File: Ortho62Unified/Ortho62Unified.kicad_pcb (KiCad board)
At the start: 2 copper layers, 300 x 140 mm, 185 parts, among them J1 AVR-PDI-6, J2 Conn_01x06_Socket, J3 USB_C_Receptacle_USB2.0, J4 Conn_01x08_Socket, J5 Conn_01x06_Socket, SW1 SW_Push, SW10 SW_Push, SW11 SW_Push, SW12 SW_Push, SW13 SW_Push, SW14 SW_Push, SW15 SW_Push, SW16 SW_Push, SW17 SW_Push, SW18 SW_Push, SW19 SW_Push, SW2 SW_Push, SW20 SW_Push, SW21 SW_Push, SW22 SW_Push, SW23 SW_Push, SW24 SW_Push, SW25 SW_Push, SW26 SW_Push, SW27 SW_Push, SW28 SW_Push, SW29 SW_Push, SW3 SW_Push, SW30 SW_Push, SW31 SW_Push, SW32 SW_Push, SW33 SW_Push, SW34 SW_Push, SW35 SW_Push, SW36 SW_Push, SW37 SW_Push, SW38 SW_Push, SW39 SW_Push, SW4 SW_Push, SW40 SW_Push, SW41 SW_Push, SW42 SW_Push, SW43 SW_Push, SW44 SW_Push, SW45 SW_Push, SW46 SW_Push, SW47 SW_Push, SW48 SW_Push, SW49 SW_Push, SW5 SW_Push, SW50 SW_Push, SW51 SW_Push, SW52 SW_Push, SW53 SW_Push, SW54 SW_Push, SW55 SW_Push, SW56 SW_Push, SW57 SW_Push, SW58 SW_Push, SW59 SW_Push, SW6 SW_Push, SW60 SW_Push, SW61 SW_Push, SW62 SW_Push, SW63 SW_Push, SW64 SW_Push, SW65 SW_Push, SW66 SW_Push, SW67 SW_Push, SW68 SW_Push, SW69 SW_Push, SW7 SW_Push, SW70 SW_Push, SW71 SW_Push, SW72 SW_Push, SW73 SW_Push, SW74 SW_Push, SW75 SW_Push, SW76 SW_Push, SW77 SW_Push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

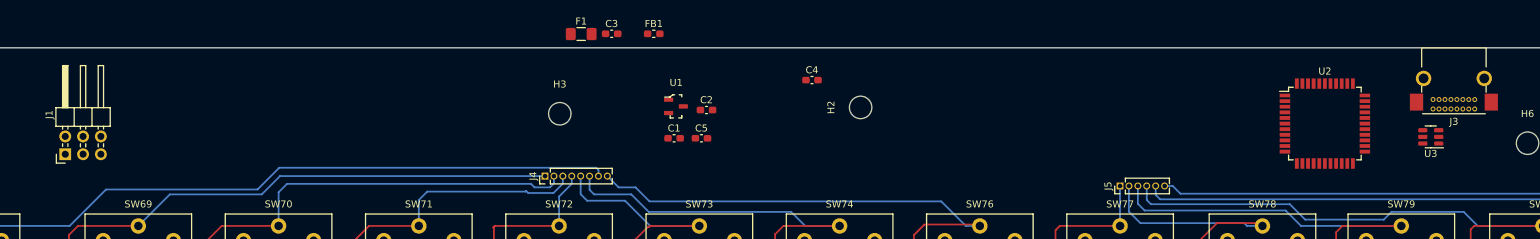
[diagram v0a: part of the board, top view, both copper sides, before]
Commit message: Consolitate and place Xmega and USB components.
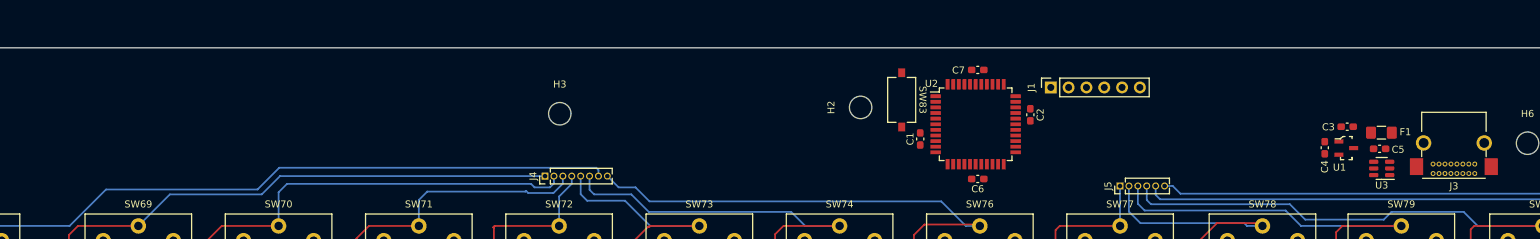
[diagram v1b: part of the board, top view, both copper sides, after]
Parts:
- removed FB1: FerriteBead, Inductor_SMD:L_0603_1608Metric_Pad1.05x0.95mm_HandSolder
- added C6: C, Capacitor_SMD:C_0603_1608Metric_Pad1.08x0.95mm_HandSolder, F.Cu at (199.6, 52.4)
- added C7: C, Capacitor_SMD:C_0603_1608Metric_Pad1.08x0.95mm_HandSolder, F.Cu at (199.6, 36.9)
- added SW83: SW_Push, Button_Switch_SMD:SW_Tactile_SPST_NO_Straight_CK_PTS636Sx25SMTRLFS, F.Cu at (188.8, 41.1)
- J1: footprint Connector_PinHeader_2.54mm:PinHeader_2x03_P2.54mm_Horizontal -> Connector_PinSocket_2.54mm:PinSocket_1x06_P2.54mm_Vertical
- moved J1 140.9 mm to (210.0, 39.4)
- moved F1 115.0 mm to (257.2, 45.8), turned to 180 degrees
- moved C3 105.7 mm to (252.3, 45.0), turned to 180 degrees
- moved C5 96.7 mm to (256.9, 48.1), turned to 180 degrees
- moved U1 95.8 mm to (252.2, 48.0)
- moved C4 73.8 mm to (249.1, 48.0), turned to 90 degrees
- moved U2 49.8 mm to (199.3, 44.6)
- moved C2 46.2 mm to (207.1, 43.2), turned to -90 degrees
- moved C1 35.1 mm to (191.4, 46.7), turned to 90 degrees
- moved J3 9.20 mm to (270.5, 51.6)
- moved U3 8.32 mm to (257.2, 50.9)
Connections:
- C2 pad 1: Net-(U2-AVCC) -> +3V3
- U2 pad 39: Net-(U2-AVCC) -> +3V3

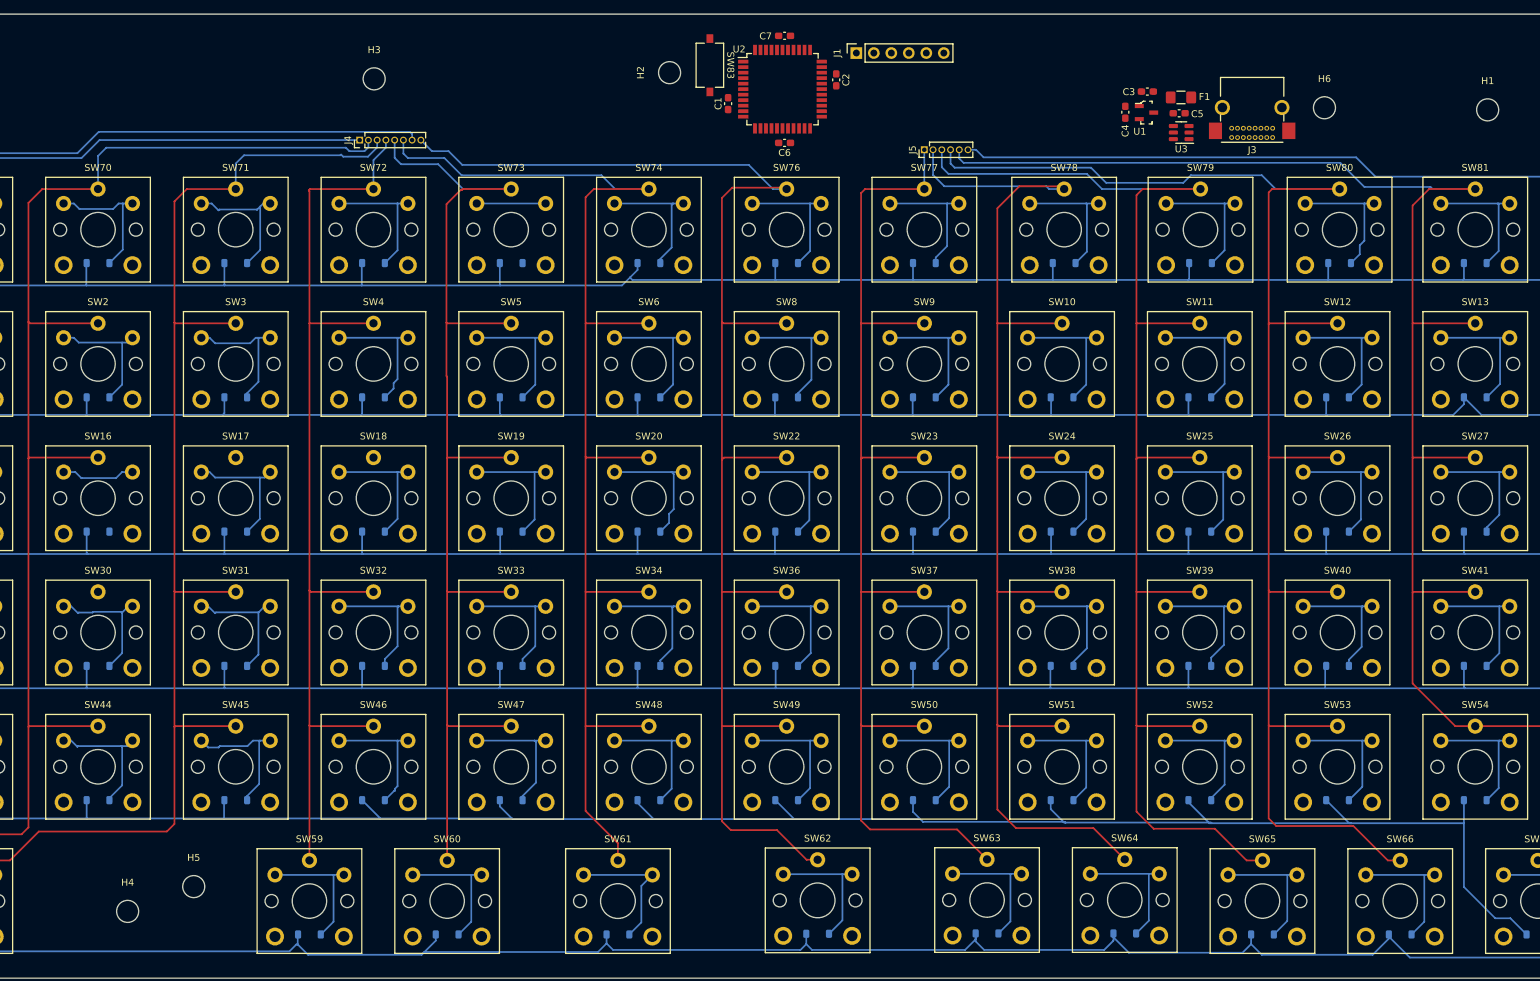
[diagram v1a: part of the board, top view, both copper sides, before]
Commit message: Remove F6,F7,F8 keys to create space for controller.
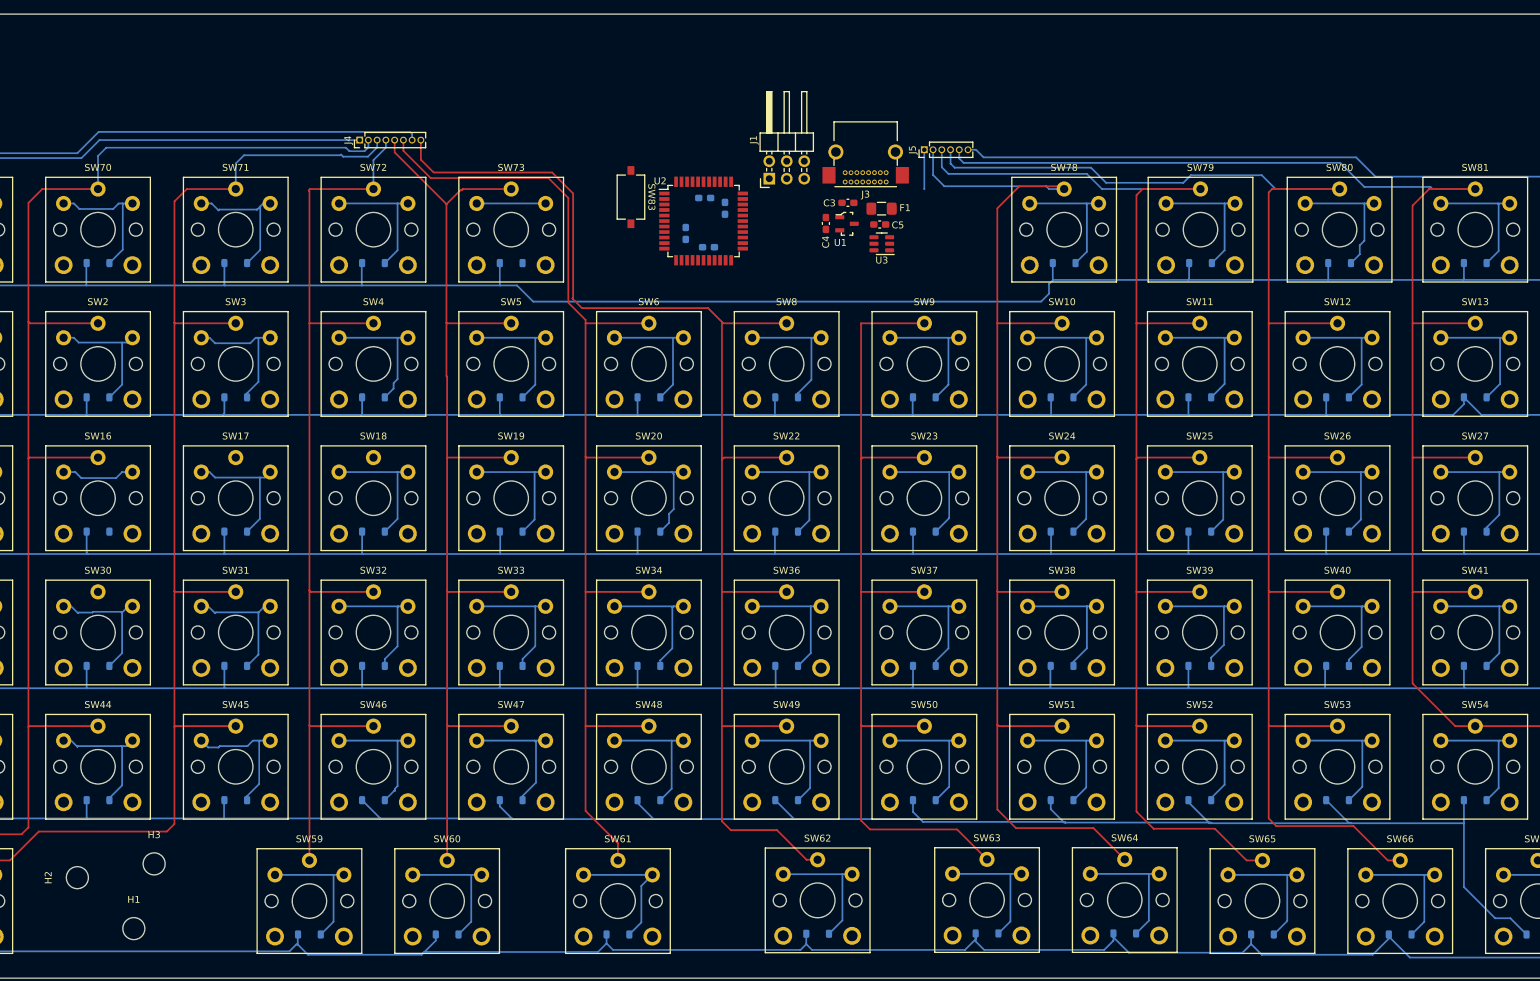
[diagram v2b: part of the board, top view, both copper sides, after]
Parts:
- removed D74, D76, D77: 1N4148W, Diode_SMD:D_SOD-123
- removed H4, H5, H6: MountingHole, MountingHole:MountingHole_3.2mm_M3
- removed SW74, SW76, SW77: SW_Push, Switch_Keyboard_Kailh:SW_Kailh_Choc_V1V2_1.00u
- C1, C2, C6, C7: moved to B.Cu
- J1: footprint Connector_PinSocket_2.54mm:PinSocket_1x06_P2.54mm_Vertical -> Connector_PinHeader_2.54mm:PinHeader_2x03_P2.54mm_Horizontal
- moved H1 229.8 mm to (105.1, 166.5)
- moved H2 145.1 mm to (96.9, 159.1)
- moved H3 118.4 mm to (108.0, 157.1)
- moved J3 56.5 mm to (214.3, 58.1)
- moved F1 46.4 mm to (213.7, 62.0)
- moved U1 46.4 mm to (208.7, 64.2)
- moved C4 46.4 mm to (205.6, 64.1)
- moved C3 46.4 mm to (208.8, 61.1)
- moved C5 46.4 mm to (213.4, 64.2)
- moved U3 46.4 mm to (213.7, 67.0)
- moved C7 26.3 mm to (188.0, 60.4)
- moved C2 24.7 mm to (190.9, 61.9)
- moved SW83 22.3 mm to (177.3, 60.3)
- moved U2 22.3 mm to (187.8, 63.8)
- moved J1 22.2 mm to (197.4, 57.6)
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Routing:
- net /COL_8: track 163.9 -> 135.5 mm
- net /COL_5: track 184.5 -> 164.4 mm
- net Net-(D74-A): track 19.4 -> 0.00 mm
- net Net-(D76-A): track 19.4 -> 0.00 mm
- net Net-(D77-A): track 19.3 -> 0.00 mm
- net /COL_7: track 210.7 -> 191.9 mm
- net /COL_4: track 164.5 -> 155.5 mm
- net /ROW_F: track 326.1 -> 321.1 mm

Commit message: Progress routing rows and columns.
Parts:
- removed J1: AVR-PDI-6, Connector_PinHeader_2.54mm:PinHeader_2x03_P2.54mm_Horizontal
- removed J4: Conn_01x08_Socket, Connector_PinHeader_1.27mm:PinHeader_1x08_P1.27mm_Vertical
- added D74: Green, LED_SMD:LED_0805_2012Metric_Pad1.15x1.40mm_HandSolder, F.Cu at (199.7, 63.7)
- added D76: Red, LED_SMD:LED_0805_2012Metric_Pad1.15x1.40mm_HandSolder, F.Cu at (179.6, 64.5)
- added J6: Conn_01x06_Socket, Connector_PinHeader_1.27mm:PinHeader_1x06_P1.27mm_Vertical, F.Cu at (186.9, 73.5)
- added J7: Conn_01x08_Socket, Connector_PinHeader_1.27mm:PinHeader_1x08_P1.27mm_Vertical, F.Cu at (172.8, 57.7)
- added J8: Conn_01x06_Socket, Connector_PinHeader_1.27mm:PinHeader_1x06_P1.27mm_Vertical, F.Cu at (196.8, 73.8)
- added J9: TC2030-IDC-NL, Tag_Connect:TC2030-IDC-NL, F.Cu at (198.3, 58.3)
- added R1: 499, Resistor_SMD:R_0805_2012Metric_Pad1.20x1.40mm_HandSolder, F.Cu at (202.2, 63.7)
- added R2: 499, LED_SMD:LED_0805_2012Metric_Pad1.15x1.40mm_HandSolder, F.Cu at (177.2, 64.4)
- moved SW83 29.5 mm to (206.8, 59.0), turned to 0 degrees
- moved J5 17.5 mm to (226.2, 69.8), turned to -90 degrees
- moved J3 8.67 mm to (222.5, 61.0)
- moved C4 1.85 mm to (205.6, 66.0)
- moved U3 1.85 mm to (213.7, 68.9)
- moved C3 1.85 mm to (208.8, 63.0)
- moved C5 1.85 mm to (213.4, 66.1)
- moved F1 1.85 mm to (213.7, 63.8)
- moved U1 1.85 mm to (208.7, 66.0)
- moved C6 1.15 mm to (188.4, 66.4)
- moved C7 0.35 mm to (188.0, 60.8)
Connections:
- J3 pad S1: unconnected-(J3-SHIELD-PadS1) -> GND
- U2 pad 1: unconnected-(U2-PA5-Pad1) -> /COL_5
- U2 pad 10: unconnected-(U2-PC0-Pad10) -> /ROW_4
- U2 pad 11: unconnected-(U2-PC1-Pad11) -> /ROW_3
- U2 pad 12: unconnected-(U2-PC2-Pad12) -> /ROW_2
- U2 pad 13: unconnected-(U2-PC3-Pad13) -> /ROW_1
- U2 pad 14: unconnected-(U2-PC4-Pad14) -> /ROW_0
- U2 pad 15: unconnected-(U2-PC5-Pad15) -> /ROW_F
- U2 pad 2: unconnected-(U2-PA6-Pad2) -> /COL_6
- U2 pad 20: unconnected-(U2-PD0-Pad20) -> /COL_8
- U2 pad 21: unconnected-(U2-PD1-Pad21) -> /COL_9
- U2 pad 22: unconnected-(U2-PD2-Pad22) -> /COL_10
- U2 pad 23: unconnected-(U2-PD3-Pad23) -> /COL_11
- U2 pad 24: unconnected-(U2-PD4-Pad24) -> /COL_12
- U2 pad 25: unconnected-(U2-PD5-Pad25) -> /COL_13
- U2 pad 3: unconnected-(U2-PA7-Pad3) -> /COL_7
- U2 pad 40: unconnected-(U2-AREFA/PA0-Pad40) -> /COL_0
- U2 pad 41: unconnected-(U2-PA1-Pad41) -> /COL_1
- U2 pad 42: unconnected-(U2-PA2-Pad42) -> /COL_2
- U2 pad 43: unconnected-(U2-PA3-Pad43) -> /COL_3
- U2 pad 44: unconnected-(U2-PA4-Pad44) -> /COL_4
- U2 pad 7: unconnected-(U2-PB3-Pad7) -> Net-(U2-PB3)
- U3 pad 1: /USB_D- -> /USB_D+
- U3 pad 3: /USB_D+ -> /USB_D-
- U3 pad 4: /USBM+ -> /USBM-
- U3 pad 6: /USBM- -> /USBM+
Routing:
- net /COL_6: track 181.7 -> 237.4 mm, vias 0 -> 2
- net /COL_0: track 202.8 -> 256.1 mm
- net +3V3: track 0.00 -> 49.8 mm, vias 0 -> 4
- net /COL_13: track 250.2 -> 294.1 mm
- net /COL_12: track 221.0 -> 262.5 mm
- net /COL_11: track 224.2 -> 264.4 mm
- net /COL_10: track 198.8 -> 238.3 mm
- net /COL_9: track 181.3 -> 219.5 mm
- net /COL_8: track 135.5 -> 168.3 mm
- net /COL_1: track 210.0 -> 180.5 mm
- net /USBM+: track 0.00 -> 21.5 mm, vias 0 -> 2
- net /USBM-: track 0.00 -> 20.7 mm
- net /COL_7: track 191.9 -> 174.5 mm
- net /COL_5: track 164.4 -> 148.2 mm
- net /COL_4: track 155.5 -> 171.4 mm, vias 0 -> 1
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- added copper zone on B.Cu, net GND
- added copper zone on F.Cu, net GND

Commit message: Routing complete for Xmega based design.
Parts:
- U1: footprint digikey-footprints:SOT-23-3 -> Package_TO_SOT_SMD:SOT-23-3
- moved SW68 0.10 mm to (329.0, 162.5)
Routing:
- net /ROW_4: track 455.2 -> 583.0 mm, vias 0 -> 2
- net /ROW_3: track 410.1 -> 514.7 mm, vias 0 -> 2
- net /COL_1: track 180.5 -> 266.6 mm
- net /ROW_2: track 398.5 -> 468.9 mm, vias 0 -> 3
- net /COL_2: track 175.9 -> 241.1 mm
- net /ROW_1: track 376.1 -> 437.3 mm, vias 0 -> 1
- net /COL_3: track 149.3 -> 195.7 mm
- net /ROW_0: track 346.8 -> 387.3 mm, vias 0 -> 1
- net Net-(D73-A): track 10.0 -> 19.4 mm
- net Net-(D16-A): track 10.8 -> 19.9 mm
- net Net-(J9-Pin_5): track 7.94 -> 17.0 mm
- net /VBUS: track 13.7 -> 19.5 mm
- net /ROW_F: track 325.3 -> 327.4 mm
- net GND: vias 11 -> 12
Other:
- board text removed: "LEFT"
- board text removed: "RIGHT"

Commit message: Add fiducials on PCB.
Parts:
- added FIDU: Fiducial_0.5mm_Mask1mm, Fiducial:Fiducial_0.5mm_Mask1mm, F.Cu at (195.0, 53.5)
- added FIDU: Fiducial_0.5mm_Mask1mm, Fiducial:Fiducial_0.5mm_Mask1mm, F.Cu at (337.5, 172.0)
- added FIDU: Fiducial_0.5mm_Mask1mm, Fiducial:Fiducial_0.5mm_Mask1mm, F.Cu at (40.5, 171.5)
- added FIDU: Fiducial_0.5mm_Mask1mm, Fiducial:Fiducial_0.5mm_Mask1mm, F.Cu at (195.0, 172.0)
- added FIDU: Fiducial_0.5mm_Mask1mm, Fiducial:Fiducial_0.5mm_Mask1mm, F.Cu at (337.5, 53.5)
- added FIDU: Fiducial_0.5mm_Mask1mm, Fiducial:Fiducial_0.5mm_Mask1mm, F.Cu at (40.5, 53.0)
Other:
- board size 300 x 140 mm -> 300 x 121.8 mm
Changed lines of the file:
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@@
     )
     (pad_to_mask_clearance 0)
-    (aux_axis_origin 97.8 39.3)
+    (aux_axis_origin 55.4 65)
+    (grid_origin 41 0)
     (pcbplotparams
       (layerselection 0x00010fc_ffffffff)
@@
     )
   )
+  (footprint "Fiducial:Fiducial_0.5mm_Mask1mm" (layer "F.Cu")
+    (at 195 53.5)
+    (descr "Circular Fiducial, 0.5mm bare copper, 1mm soldermask opening (Level C)")
+    (tags "fiducial")
+    (attr smd)
+    (fp_text reference "FIDU" (at 3 0) (layer "F.SilkS")
+        (effects (font (size 1 1) (thickness 0.15)))
+    )
+    (fp_text value "Fiducial_0.5mm_Mask1mm" (at 0 1.5) (layer "F.Fab")
+        (effects (font (size 1 1) (thickness 0.15)))
+    )
+    (fp_text user "${REFERENCE}" (at 0 0) (layer "F.Fab")
+        (effects (font (size 0.2 0.2) (thickness 0.04)))
+    )
+    (fp_circle (center 0 0) (end 0.75 0)
+      (stroke (width 0.05) (type solid)) (fill none) (layer "F.CrtYd"))
+    (fp_circle (center 0 0) (end 0.5 0)
+      (stroke (width 0.1) (type solid)) (fill none) (layer "F.Fab"))
+    (pad "" smd circle (at 0 0) (size 0.5 0.5) (layers "F.Cu" "F.Mask")
+      (solder_mask_margin 0.25) (clearance 0.25))
+  )
   (footprint "Switch_Keyboard_Kailh:SW_Kailh_Choc_V1V2_1.00u" (layer "F.Cu")
     (at 99.9 65)
@@
     )
   )
+  (footprint "Fiducial:Fiducial_0.5mm_Mask1mm" (layer "F.Cu")
+    (at 337.5 172)
+    (descr "Circular Fiducial, 0.5mm bare copper, 1mm soldermask opening (Level C)")
+    (tags "fiducial")
+    (attr smd)
+    (fp_text reference "FIDU" (at -2.5 0) (layer "F.SilkS")
+        (effects (font (size 1 1) (thickness 0.15)))
+    )
+    (fp_text value "Fiducial_0.5mm_Mask1mm" (at 0 1.5) (layer "F.Fab")
+        (effects (font (size 1 1) (thickness 0.15)))
+    )
+    (fp_text user "${REFERENCE}" (at 0 0) (layer "F.Fab")
+        (effects (font (size 0.2 0.2) (thickness 0.04)))
+    )
+    (fp_circle (center 0 0) (end 0.75 0)
+      (stroke (width 0.05) (type solid)) (fill none) (layer "F.CrtYd"))
+    (fp_circle (center 0 0) (end 0.5 0)
+      (stroke (width 0.1) (type solid)) (fill none) (layer "F.Fab"))
+    (pad "" smd circle (at 0 0) (size 0.5 0.5) (layers "F.Cu" "F.Mask")
+      (solder_mask_margin 0.25) (clearance 0.25))
+  )
   (footprint "Switch_Keyboard_Kailh:SW_Kailh_Choc_V1V2_1.00u" (layer "F.Cu")
     (at 329 162.5)
@@
     )
   )
+  (footprint "Fiducial:Fiducial_0.5mm_Mask1mm" (layer "F.Cu")
+    (at 40.5 171.5)
+    (descr "Circular Fiducial, 0.5mm bare copper, 1mm soldermask opening (Level C)")
+    (tags "fiducial")
+    (attr smd)
+    (fp_text reference "FIDU" (at 3 0) (layer "F.SilkS")
+        (effects (font (size 1 1) (thickness 0.15)))
+    )
+    (fp_text value "Fiducial_0.5mm_Mask1mm" (at 0 1.5) (layer "F.Fab")
+        (effects (font (size 1 1) (thickness 0.15)))
+    )
+    (fp_text user "${REFERENCE}" (at 0 0) (layer "F.Fab")
+        (effects (font (size 0.2 0.2) (thickness 0.04)))
+    )
+    (fp_circle (center 0 0) (end 0.75 0)
+      (stroke (width 0.05) (type solid)) (fill none) (layer "F.CrtYd"))
+    (fp_circle (center 0 0) (end 0.5 0)
+      (stroke (width 0.1) (type solid)) (fill none) (layer "F.Fab"))
+    (pad "" smd circle (at 0 0) (size 0.5 0.5) (layers "F.Cu" "F.Mask")
+      (solder_mask_margin 0.25) (clearance 0.25))
+  )
   (footprint "LED_SMD:LED_0805_2012Metric_Pad1.15x1.40mm_HandSolder" (layer "F.Cu")
     (at 179.6 64.45 -90)
@@
     )
   )
+  (footprint "Fiducial:Fiducial_0.5mm_Mask1mm" (layer "F.Cu")
+    (at 195 172)
+    (descr "Circular Fiducial, 0.5mm bare copper, 1mm soldermask opening (Level C)")
+    (tags "fiducial")
+    (attr smd)
+    (fp_text reference "FIDU" (at -2.5 0) (layer "F.SilkS")
+        (effects (font (size 1 1) (thickness 0.15)))
+    )
+    (fp_text value "Fiducial_0.5mm_Mask1mm" (at 0 1.5) (layer "F.Fab")
+        (effects (font (size 1 1) (thickness 0.15)))
+    )
+    (fp_text user "${REFERENCE}" (at 0 0) (layer "F.Fab")
+        (effects (font (size 0.2 0.2) (thickness 0.04)))
+    )
+    (fp_circle (center 0 0) (end 0.75 0)
+      (stroke (width 0.05) (type solid)) (fill none) (layer "F.CrtYd"))
+    (fp_circle (center 0 0) (end 0.5 0)
+      (stroke (width 0.1) (type solid)) (fill none) (layer "F.Fab"))
+    (pad "" smd circle (at 0 0) (size 0.5 0.5) (layers "F.Cu" "F.Mask")
+      (solder_mask_margin 0.25) (clearance 0.25))
+  )
   (footprint "Switch_Keyboard_Kailh:SW_Kailh_Choc_V1V2_1.00u" (layer "F.Cu")
     (at 240.2 65)
@@
     )
   )
+  (footprint "Fiducial:Fiducial_0.5mm_Mask1mm" (layer "F.Cu")
+    (at 337.5 53.5)
+    (descr "Circular Fiducial, 0.5mm bare copper, 1mm soldermask opening (Level C)")
+    (tags "fiducial")
+    (attr smd)
+    (fp_text reference "FIDU" (at -3 0) (layer "F.SilkS")
+        (effects (font (size 1 1) (thickness 0.15)))
+    )
+    (fp_text value "Fiducial_0.5mm_Mask1mm" (at 0 1.5) (layer "F.Fab")
+        (effects (font (size 1 1) (thickness 0.15)))
+    )
+    (fp_text user "${REFERENCE}" (at 0 0) (layer "F.Fab")
+        (effects (font (size 0.2 0.2) (thickness 0.04)))
+    )
+    (fp_circle (center 0 0) (end 0.75 0)
+      (stroke (width 0.05) (type solid)) (fill none) (layer "F.CrtYd"))
+    (fp_circle (center 0 0) (end 0.5 0)
+      (stroke (width 0.1) (type solid)) (fill none) (layer "F.Fab"))
+    (pad "" smd circle (at 0 0) (size 0.5 0.5) (layers "F.Cu" "F.Mask")
+      (solder_mask_margin 0.25) (clearance 0.25))
+  )
   (footprint "MountingHole:MountingHole_3.2mm_M3" (layer "F.Cu")
     (at 108.05 157.1)
@@
     )
   )
+  (footprint "Fiducial:Fiducial_0.5mm_Mask1mm" (layer "F.Cu")
+    (at 40.5 53)
+    (descr "Circular Fiducial, 0.5mm bare copper, 1mm soldermask opening (Level C)")
+    (tags "fiducial")
+    (attr smd)
+    (fp_text reference "FIDU" (at 0 2.5 90) (layer "F.SilkS")
+        (effects (font (size 1 1) (thickness 0.15)))
+    )
+    (fp_text value "Fiducial_0.5mm_Mask1mm" (at 0 1.5) (layer "F.Fab")
+        (effects (font (size 1 1) (thickness 0.15)))
+    )
+    (fp_text user "${REFERENCE}" (at 0 0) (layer "F.Fab")
+        (effects (font (size 0.2 0.2) (thickness 0.04)))
+    )
+    (fp_circle (center 0 0) (end 0.75 0)
+      (stroke (width 0.05) (type solid)) (fill none) (layer "F.CrtYd"))
+    (fp_circle (center 0 0) (end 0.5 0)
+      (stroke (width 0.1) (type solid)) (fill none) (layer "F.Fab"))
+    (pad "" smd circle (at 0 0) (size 0.5 0.5) (layers "F.Cu" "F.Mask")
+      (solder_mask_margin 0.25) (clearance 0.25))
+  )
   (footprint "MountingHole:MountingHole_3.2mm_M3" (layer "F.Cu")
     (at 96.9 159.1 90)
@@
     )
   )
-  (gr_rect (start 39.6 33.7) (end 339.6 173.7)
+  (gr_rect (start 39.6 51.9) (end 339.6 173.7)
     (stroke (width 0.1) (type default)) (fill none) (layer "Edge.Cuts"))
   (gr_text "MacSplit66 Keyboard by Neeraj Adsul\nCopyright 2022, 125 Systems.\nRevision 1" (at 242.8 46.6) (layer "F.Fab")
